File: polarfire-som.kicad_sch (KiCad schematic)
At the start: 0 parts

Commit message: [#52579] Connect signals to SoC
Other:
- added sheet Connectors (connectors.kicad_sch)
- added sheet LPDDR4 (lpddr.kicad_sch)
- added sheet Misc (misc.kicad_sch)
- added sheet PCIe (pcie.kicad_sch)
- added sheet SoC (soc.kicad_sch)
- added sheet Supply (supply.kicad_sch)
- added sheet USB (usb.kicad_sch)
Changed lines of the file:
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@@
     (comment 1 "www.antmicro.com")
+  )
+  (sheet (at 209.55 135.89) (size 26.67 17.78) (fields_autoplaced)
+    (stroke (width 0.1524) (type solid) (color 0 0 0 0))
+    (fill (color 0 0 0 0.0000))
+    (property "Sheet name" "LPDDR4" (id 0) (at 209.55 135.1784 0)
+      (effects (font (size 1.27 1.27)) (justify left bottom))
+    )
+    (property "Sheet file" "lpddr.kicad_sch" (id 1) (at 209.55 154.2546 0)
+      (effects (font (size 1.27 1.27)) (justify left top))
+    )
+  )
+  (sheet (at 52.07 135.89) (size 26.67 17.78) (fields_autoplaced)
+    (stroke (width 0.1524) (type solid) (color 0 0 0 0))
+    (fill (color 0 0 0 0.0000))
+    (property "Sheet name" "Connectors" (id 0) (at 52.07 135.1784 0)
+      (effects (font (size 1.27 1.27)) (justify left bottom))
+    )
+    (property "Sheet file" "connectors.kicad_sch" (id 1) (at 52.07 154.2546 0)
+      (effects (font (size 1.27 1.27)) (justify left top))
+    )
+  )
+  (sheet (at 130.81 135.89) (size 26.67 17.78) (fields_autoplaced)
+    (stroke (width 0.1524) (type solid) (color 0 0 0 0))
+    (fill (color 0 0 0 0.0000))
+    (property "Sheet name" "Misc" (id 0) (at 130.81 135.1784 0)
+      (effects (font (size 1.27 1.27)) (justify left bottom))
+    )
+    (property "Sheet file" "misc.kicad_sch" (id 1) (at 130.81 154.2546 0)
+      (effects (font (size 1.27 1.27)) (justify left top))
+    )
+  )
+  (sheet (at 91.44 135.89) (size 26.67 17.78) (fields_autoplaced)
+    (stroke (width 0.1524) (type solid) (color 0 0 0 0))
+    (fill (color 0 0 0 0.0000))
+    (property "Sheet name" "SoC" (id 0) (at 91.44 135.1784 0)
+      (effects (font (size 1.27 1.27)) (justify left bottom))
+    )
+    (property "Sheet file" "soc.kicad_sch" (id 1) (at 91.44 154.2546 0)
+      (effects (font (size 1.27 1.27)) (justify left top))
+    )
+  )
+  (sheet (at 170.18 135.89) (size 26.67 17.78) (fields_autoplaced)
+    (stroke (width 0.1524) (type solid) (color 0 0 0 0))
+    (fill (color 0 0 0 0.0000))
+    (property "Sheet name" "Supply" (id 0) (at 170.18 135.1784 0)
+      (effects (font (size 1.27 1.27)) (justify left bottom))
+    )
+    (property "Sheet file" "supply.kicad_sch" (id 1) (at 170.18 154.2546 0)
+      (effects (font (size 1.27 1.27)) (justify left top))
+    )
+  )
+  (sheet (at 91.44 107.95) (size 26.67 17.78) (fields_autoplaced)
+    (stroke (width 0.1524) (type solid) (color 0 0 0 0))
+    (fill (color 0 0 0 0.0000))
+    (property "Sheet name" "PCIe" (id 0) (at 91.44 107.2384 0)
+      (effects (font (size 1.27 1.27)) (justify left bottom))
+    )
+    (property "Sheet file" "pcie.kicad_sch" (id 1) (at 91.44 126.3146 0)
+      (effects (font (size 1.27 1.27)) (justify left top))
+    )
+  )
+  (sheet (at 52.07 107.95) (size 26.67 17.78) (fields_autoplaced)
+    (stroke (width 0.1524) (type solid) (color 0 0 0 0))
+    (fill (color 0 0 0 0.0000))
+    (property "Sheet name" "USB" (id 0) (at 52.07 107.2384 0)
+      (effects (font (size 1.27 1.27)) (justify left bottom))
+    )
+    (property "Sheet file" "usb.kicad_sch" (id 1) (at 52.07 126.3146 0)
+      (effects (font (size 1.27 1.27)) (justify left top))
+    )
   )
   (sheet_instances
     (path "/" (page "1"))
+    (path "/1a89b4c6-5d95-4c13-8da9-62b42c0a8ed9" (page "2"))
+    (path "/99f116ae-bc8e-42a5-8f88-aecc401b3bcc" (page "3"))
+    (path "/6b5c9386-08fc-46bf-a582-c320c1d104da" (page "4"))
+    (path "/aa0aa716-c477-450b-ad01-6403345c3aae" (page "5"))
+    (path "/03c99aa2-3a70-4e62-834d-8bf1b61d2c0d" (page "6"))
+    (path "/d93d65d4-e21e-44e3-82fb-4ad52468a6b3" (page "7"))
+    (path "/c9bdf952-cb44-4ee1-a4b1-ef79b2174bdb" (page "8"))
+  )
+  (symbol_instances
+    (path "/1a89b4c6-5d95-4c13-8da9-62b42c0a8ed9/a5fb86dc-a7eb-4dbf-a831-b4bb59ec38f4"
+      (reference "#PWR?") (unit 1) (value "GND") (footprint "")
+    )
+    (path "/1a89b4c6-5d95-4c13-8da9-62b42c0a8ed9/b07c68a4-4958-4293-babe-6dfd9512ec03"
+      (reference "#PWR?") (unit 1) (value "GND") (footprint "")
+    )
+    (path "/1a89b4c6-5d95-4c13-8da9-62b42c0a8ed9/b6e07bd8-c529-406a-8663-c7db69baf72d"
+      (reference "#PWR?") (unit 1) (value "GND") (footprint "")
+    )
+    (path "/1a89b4c6-5d95-4c13-8da9-62b42c0a8ed9/c410c1e5-46b2-4389-ae78-de86c508cca9"
+      (reference "#PWR?") (unit 1) (value "GND") (footprint "")
+    )
+    (path "/1a89b4c6-5d95-4c13-8da9-62b42c0a8ed9/ab4369a7-e4e8-43db-a719-65d5abf7c44e"
+      (reference "J?") (unit 1) (value "CM4_Plug_Module_Hirose_DF40_2x50_DF40C-100DP-0.4V_1") (footprint "antmicro-footprints:CM4_Module_Conn_Plug_Hirose_DF40_2x50_DF40C-100DP-0.4V")
+    )
+    (path "/1a89b4c6-5d95-4c13-8da9-62b42c0a8ed9/a6694df8-ade9-452b-bc07-4b7bc818e782"
+      (reference "J?") (unit 2) (value "CM4_Plug_Module_Hirose_DF40_2x50_DF40C-100DP-0.4V_1") (footprint "antmicro-footprints:CM4_Module_Conn_Plug_Hirose_DF40_2x50_DF40C-100DP-0.4V")
+    )
+    (path "/99f116ae-bc8e-42a5-8f88-aecc401b3bcc/48b961bb-e84f-4162-9b4f-ee3835cef348"
+      (reference "U?") (unit 1) (value "MPFS250T-FCVG484") (footprint "antmicro-footprints:BGA-484_19x19mm_Layout22x22_P0.8mm_FCVG484")
+    )
+    (path "/6b5c9386-08fc-46bf-a582-c320c1d104da/5187db4b-d539-45e7-9e51-971745f66849"
+      (reference "U?") (unit 1) (value "SDINBDG4-8G") (footprint "antmicro-footprints:BGA-196-153_11.5x13mm_Layout14x14_P0.5x0.5mm")
+    )
+    (path "/d93d65d4-e21e-44e3-82fb-4ad52468a6b3/b5c33554-f489-40de-90a8-a44de066fed2"
+      (reference "U?") (unit 1) (value "USB3300-EZK-TR") (footprint "antmicro-footprints:QFN-32-1EP_5x5mm")
+    )
+    (path "/6b5c9386-08fc-46bf-a582-c320c1d104da/c6bf1eab-4fb6-4f61-ae8e-24d235924fe7"
+      (reference "U?") (unit 1) (value "KSZ9031RNXCA") (footprint "antmicro-footprints:QFN-48-1EP_7x7x0.9mm_P0.5mm_EP3.5x3.5mm")
+    )
+    (path "/03c99aa2-3a70-4e62-834d-8bf1b61d2c0d/f40a1270-ecf4-4442-abdc-af92e672eb72"
+      (reference "U?") (unit 1) (value "MT53D512M32D2_WFBGA") (footprint "antmicro-footprints:BGA-200_10.0x14.5mm_Layout12x22_P0.80x0.65mm")
+    )
+    (path "/03c99aa2-3a70-4e62-834d-8bf1b61d2c0d/0861c16c-4e53-4ec4-9218-e0d59d09c43e"
+      (reference "U?") (unit 2) (value "MT53D512M32D2_WFBGA") (footprint "antmicro-footprints:BGA-200_10.0x14.5mm_Layout12x22_P0.80x0.65mm")
+    )
+    (path "/99f116ae-bc8e-42a5-8f88-aecc401b3bcc/33525ff0-ccdb-444b-b19d-33f381d75f01"
+      (reference "U?") (unit 2) (value "MPFS250T-FCVG484") (footprint "antmicro-footprints:BGA-484_19x19mm_Layout22x22_P0.8mm_FCVG484")
+    )
+    (path "/d93d65d4-e21e-44e3-82fb-4ad52468a6b3/a36f6da2-98d9-4ec9-ae8a-0cc3f93b6e54"
+      (reference "U?") (unit 3) (value "MPFS250T-FCVG484") (footprint "antmicro-footprints:BGA-484_19x19mm_Layout22x22_P0.8mm_FCVG484")
+    )
+    (path "/99f116ae-bc8e-42a5-8f88-aecc401b3bcc/01a8e936-ac00-46aa-bdec-90f3e2fa7dcd"
+      (reference "U?") (unit 4) (value "MPFS250T-FCVG484") (footprint "antmicro-footprints:BGA-484_19x19mm_Layout22x22_P0.8mm_FCVG484")
+    )
+    (path "/6b5c9386-08fc-46bf-a582-c320c1d104da/4df2db3b-10de-4c55-ac4b-f4970c27fdb0"
+      (reference "U?") (unit 5) (value "MPFS250T-FCVG484") (footprint "antmicro-footprints:BGA-484_19x19mm_Layout22x22_P0.8mm_FCVG484")
+    )
+    (path "/6b5c9386-08fc-46bf-a582-c320c1d104da/cea481a3-fb30-453b-b323-af909851807a"
+      (reference "U?") (unit 6) (value "MPFS250T-FCVG484") (footprint "antmicro-footprints:BGA-484_19x19mm_Layout22x22_P0.8mm_FCVG484")
+    )
+    (path "/03c99aa2-3a70-4e62-834d-8bf1b61d2c0d/ed7fecde-3f9c-495d-9fe5-03c9de60dcbd"
+      (reference "U?") (unit 7) (value "MPFS250T-FCVG484") (footprint "antmicro-footprints:BGA-484_19x19mm_Layout22x22_P0.8mm_FCVG484")
+    )
+    (path "/c9bdf952-cb44-4ee1-a4b1-ef79b2174bdb/d8a6074a-58a3-41a8-8dfe-d1bf155a41bc"
+      (reference "U?") (unit 8) (value "MPFS250T-FCVG484") (footprint "antmicro-footprints:BGA-484_19x19mm_Layout22x22_P0.8mm_FCVG484")
+    )
+    (path "/99f116ae-bc8e-42a5-8f88-aecc401b3bcc/1777c82a-f68b-42ff-9d15-9c98b18f3de1"
+      (reference "U?") (unit 9) (value "MPFS250T-FCVG484") (footprint "antmicro-footprints:BGA-484_19x19mm_Layout22x22_P0.8mm_FCVG484")
+    )
   )
 )

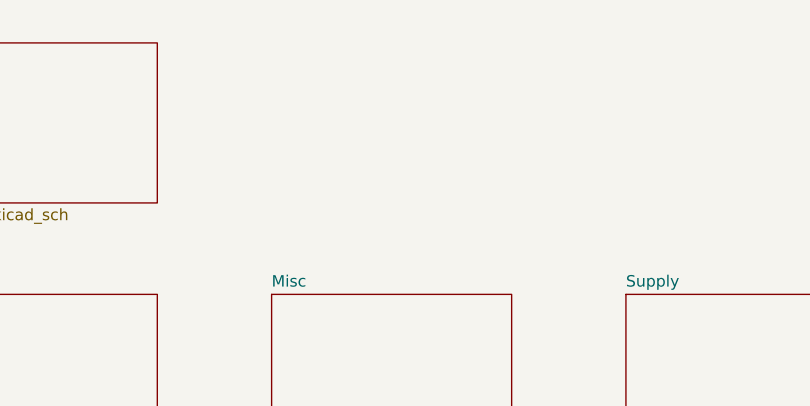
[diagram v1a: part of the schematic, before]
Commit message: [#52579] WiP: Add CrossLink to schematic
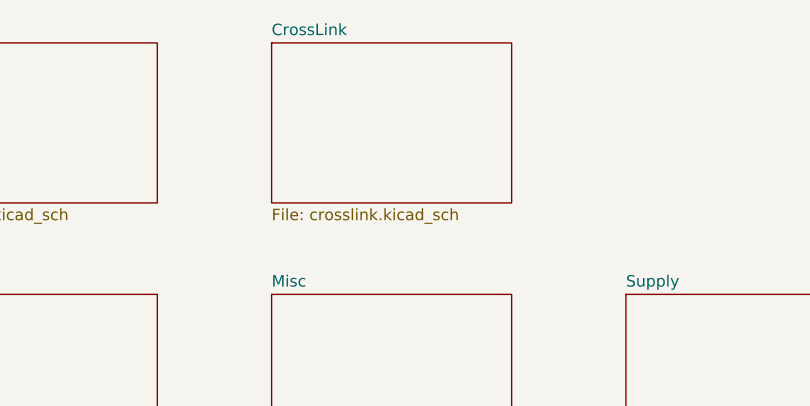
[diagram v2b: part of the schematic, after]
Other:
- added sheet CrossLink (crosslink.kicad_sch)
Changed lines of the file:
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@@
+    )
+  )
+  (sheet (at 130.81 107.95) (size 26.67 17.78) (fields_autoplaced)
+    (stroke (width 0.1524) (type solid) (color 0 0 0 0))
+    (fill (color 0 0 0 0.0000))
+    (property "Sheet name" "CrossLink" (id 0) (at 130.81 107.2384 0)
+      (effects (font (size 1.27 1.27)) (justify left bottom))
+    )
+    (property "Sheet file" "crosslink.kicad_sch" (id 1) (at 130.81 126.3146 0)
+      (effects (font (size 1.27 1.27)) (justify left top))
     )
   )
@@
     (path "/d93d65d4-e21e-44e3-82fb-4ad52468a6b3" (page "7"))
     (path "/c9bdf952-cb44-4ee1-a4b1-ef79b2174bdb" (page "8"))
+    (path "/c4778e63-1261-4544-aaba-813aa24c5b7b" (page "9"))
   )
   (symbol_instances
@@
       (reference "U?") (unit 1) (value "SDINBDG4-8G") (footprint "antmicro-footprints:BGA-196-153_11.5x13mm_Layout14x14_P0.5x0.5mm")
     )
+    (path "/c4778e63-1261-4544-aaba-813aa24c5b7b/936d1e6c-dd8a-4d25-9d12-6b0369f305b2"
+      (reference "U?") (unit 1) (value "CrossLink_LIF-MD6000-6JMG80I") (footprint "antmicro-footprints:BGA-80_7x7mm_Layout10x10_P0.65mm")
+    )
     (path "/d93d65d4-e21e-44e3-82fb-4ad52468a6b3/b5c33554-f489-40de-90a8-a44de066fed2"

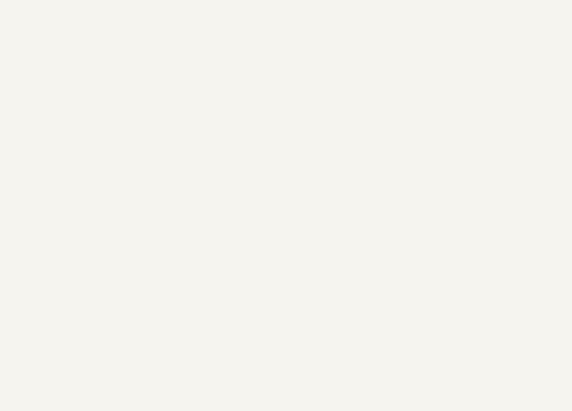
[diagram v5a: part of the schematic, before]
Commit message: [#52579] Create initial components layout
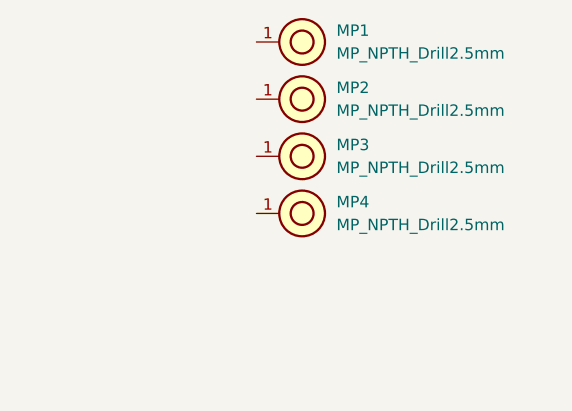
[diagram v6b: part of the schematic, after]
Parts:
- added MP1, MP2, MP3, MP4: MP_NPTH_Drill2.5mm, antmicro-footprints:MP_NPTH_Drill2.5mm, symbol antmicroMechanicalParts:MP_NPTH_Drill2.5mm

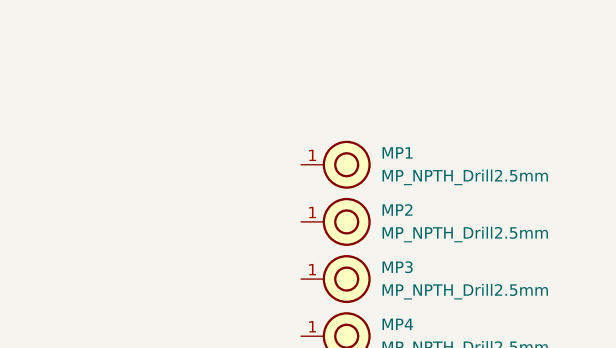
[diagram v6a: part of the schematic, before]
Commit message: [#52579] Add Antmicro and OSHW logo
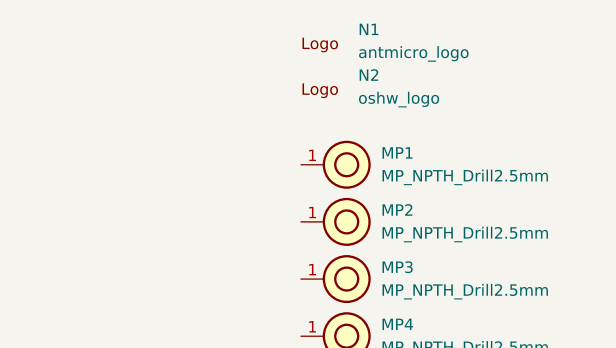
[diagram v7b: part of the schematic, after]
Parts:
- added N1: antmicro_logo, antmicro-footprints:antmicro-logo_scaled_12mm, symbol antmicroMechanicalParts:antmicro_logo
- added N2: oshw_logo, antmicro-footprints:oshw-logo, symbol antmicroMechanicalParts:oshw_logo
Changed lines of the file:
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@@
     (pin "1")
+  )
+  (symbol (lib_id "antmicroMechanicalParts:oshw_logo") (at 219.71 81.28 0) (unit 1)
+    (in_bom no) (on_board yes) (fields_autoplaced)
+    (property "Reference" "N2" (id 0) (at 226.06 78.9875 0)
+      (effects (font (size 1.27 1.27) (thickness 0.15)) (justify left))
+    )
+    (property "Value" "oshw_logo" (id 1) (at 226.06 81.5275 0)
+      (effects (font (size 1.27 1.27) (thickness 0.15)) (justify left))
+    )
+    (property "Footprint" "antmicro-footprints:oshw-logo" (id 2) (at 234.95 91.44 0)
+      (effects (font (size 1.27 1.27) (thickness 0.15)) (justify left bottom) hide)
+    )
+    (property "Datasheet" "" (id 3) (at 234.95 93.98 0)
+      (effects (font (size 1.27 1.27) (thickness 0.15)) (justify left bottom) hide)
+    )
+    (property "Author" "Antmicro" (id 4) (at 234.95 96.52 0)
+      (effects (font (size 1.27 1.27) (thickness 0.15)) (justify left bottom) hide)
+    )
+    (property "License" "Apache-2.0" (id 5) (at 234.95 99.06 0)
+      (effects (font (size 1.27 1.27) (thickness 0.15)) (justify left bottom) hide)
+    )
+    (property "MPN" "" (id 6) (at 219.71 81.28 0)
+      (effects (font (size 1.27 1.27)) hide)
+    )
+    (property "Manufacturer" "" (id 7) (at 234.95 101.6 0)
+      (effects (font (size 1.27 1.27) (thickness 0.15)) (justify left bottom) hide)
+    )
   )
   (symbol (lib_id "antmicroMechanicalParts:MP_NPTH_Drill2.5mm") (at 219.71 107.95 0) (unit 1)
@@
     )
     (pin "1")
+  )
+  (symbol (lib_id "antmicroMechanicalParts:antmicro_logo") (at 219.71 76.2 0) (unit 1)
+    (in_bom no) (on_board yes) (fields_autoplaced)
+    (property "Reference" "N1" (id 0) (at 226.06 73.9075 0)
+      (effects (font (size 1.27 1.27) (thickness 0.15)) (justify left))
+    )
+    (property "Value" "antmicro_logo" (id 1) (at 226.06 76.4475 0)
+      (effects (font (size 1.27 1.27) (thickness 0.15)) (justify left))
+    )
+    (property "Footprint" "antmicro-footprints:antmicro-logo_scaled_12mm" (id 2) (at 234.95 86.36 0)
+      (effects (font (size 1.27 1.27) (thickness 0.15)) (justify left bottom) hide)
+    )
+    (property "Datasheet" "" (id 3) (at 234.95 88.9 0)
+      (effects (font (size 1.27 1.27) (thickness 0.15)) (justify left bottom) hide)
+    )
+    (property "MPN" "" (id 4) (at 219.71 76.2 0)
+      (effects (font (size 1.27 1.27)) hide)
+    )
+    (property "Manufacturer" "" (id 5) (at 234.95 96.52 0)
+      (effects (font (size 1.27 1.27) (thickness 0.15)) (justify left bottom) hide)
+    )
+    (property "Author" "Antmicro" (id 6) (at 234.95 91.44 0)
+      (effects (font (size 1.27 1.27) (thickness 0.15)) (justify left bottom) hide)
+    )
+    (property "License" "Apache-2.0" (id 7) (at 234.95 93.98 0)
+      (effects (font (size 1.27 1.27) (thickness 0.15)) (justify left bottom) hide)
+    )
   )
   (symbol (lib_id "antmicroMechanicalParts:MP_NPTH_Drill2.5mm") (at 219.71 95.25 0) (unit 1)
@@
       (reference "MP4") (unit 1) (value "MP_NPTH_Drill2.5mm") (footprint "antmicro-footprints:MP_NPTH_Drill2.5mm")
     )
+    (path "/a2fd1a52-2d23-412d-b7b5-b05cd3a0bc42"
+      (reference "N1") (unit 1) (value "antmicro_logo") (footprint "antmicro-footprints:antmicro-logo_scaled_12mm")
+    )
+    (path "/8206b603-1e7e-4eeb-8094-4d4b0c2e7e41"
+      (reference "N2") (unit 1) (value "oshw_logo") (footprint "antmicro-footprints:oshw-logo")
+    )
     (path "/99f116ae-bc8e-42a5-8f88-aecc401b3bcc/48b961bb-e84f-4162-9b4f-ee3835cef348"

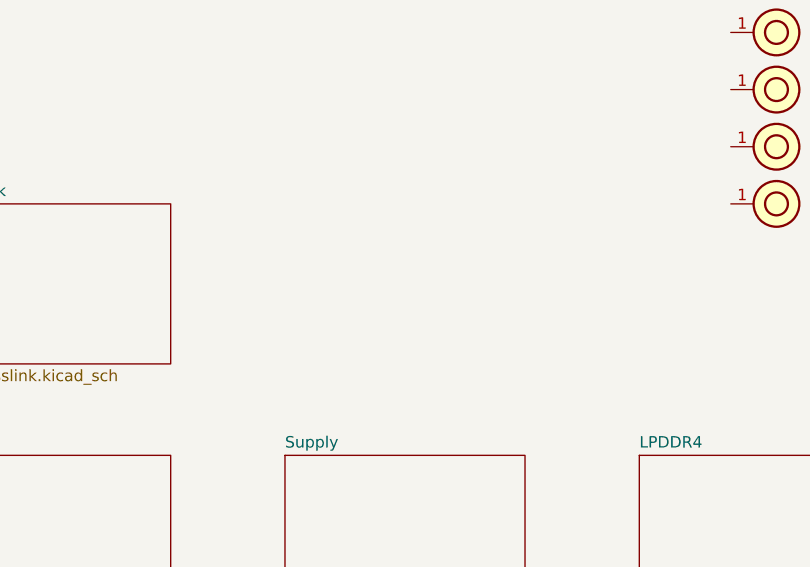
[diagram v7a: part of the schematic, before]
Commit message: [#53847] Add TPD12S016 and connect HDMI to pfsom
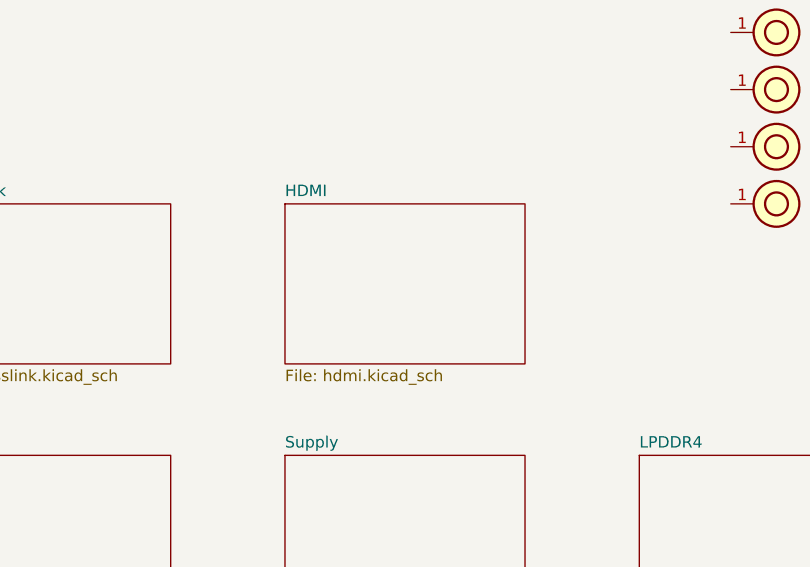
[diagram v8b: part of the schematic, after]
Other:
- added sheet HDMI (hdmi.kicad_sch)
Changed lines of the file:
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@@
+    )
+  )
+  (sheet (at 170.18 107.95) (size 26.67 17.78) (fields_autoplaced)
+    (stroke (width 0.1524) (type solid) (color 0 0 0 0))
+    (fill (color 0 0 0 0.0000))
+    (property "Sheet name" "HDMI" (id 0) (at 170.18 107.2384 0)
+      (effects (font (size 1.27 1.27)) (justify left bottom))
+    )
+    (property "Sheet file" "hdmi.kicad_sch" (id 1) (at 170.18 126.3146 0)
+      (effects (font (size 1.27 1.27)) (justify left top))
     )
   )
@@
     (path "/c9bdf952-cb44-4ee1-a4b1-ef79b2174bdb" (page "8"))
     (path "/c4778e63-1261-4544-aaba-813aa24c5b7b" (page "9"))
+    (path "/9d03ca8b-00f4-4bc6-89d1-f3be2c1a83b3" (page "10"))
   )
   (symbol_instances
@@
       (reference "U9") (unit 1) (value "CrossLink_LIF-MD6000-6JMG80I") (footprint "antmicro-footprints:BGA-80_7x7mm_Layout10x10_P0.65mm")
     )
+    (path "/9d03ca8b-00f4-4bc6-89d1-f3be2c1a83b3/6b7beb5c-67ba-4dca-8603-d8ff078ad5d4"
+      (reference "U?") (unit 1) (value "TPD12S016_QFN") (footprint "antmicro-footprints:UQFN-24_2x4mm_Layout2x10")
+    )
   )
